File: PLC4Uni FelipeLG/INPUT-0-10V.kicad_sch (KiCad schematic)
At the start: 3 parts

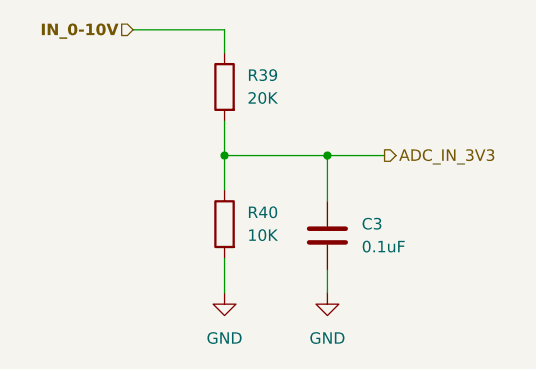
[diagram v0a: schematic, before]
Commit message: Add files via upload
Updated Circuitos corregidos y pistas agregadas
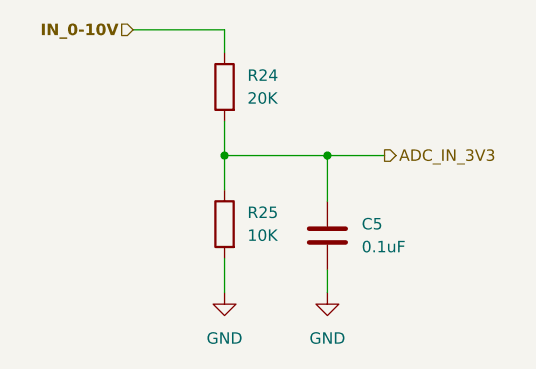
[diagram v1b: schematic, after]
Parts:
- renumbered C3 to C5, R39 to R24, R40 to R25
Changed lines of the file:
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@@
 		(dnp no)
 		(fields_autoplaced yes)
-		(property "Reference" "#PWR04"
+		(property "Reference" "#PWR049"
 			(at 133.35 121.92 0)
 			(effects
@@
 			(project "Diseños de circuitos"
 				(path "/65c875c0-73bd-43df-b6cd-4a685398cace/3b453a73-5bb7-4645-a7e8-6e186968fa05/26d79baa-0338-43a5-b3e5-bc5aeada5ecf"
-					(reference "#PWR04")
+					(reference "#PWR049")
 					(unit 1)
 				)
@@
 		(dnp no)
 		(fields_autoplaced yes)
-		(property "Reference" "R40"
+		(property "Reference" "R25"
 			(at 124.46 106.6799 0)
 			(effects
@@
 			(project "Diseños de circuitos"
 				(path "/65c875c0-73bd-43df-b6cd-4a685398cace/3b453a73-5bb7-4645-a7e8-6e186968fa05/26d79baa-0338-43a5-b3e5-bc5aeada5ecf"
-					(reference "R40")
+					(reference "R25")
 					(unit 1)
 				)
@@
 		(dnp no)
 		(fields_autoplaced yes)
-		(property "Reference" "R39"
+		(property "Reference" "R24"
 			(at 124.46 91.4399 0)
 			(effects
@@
 			(project "Diseños de circuitos"
 				(path "/65c875c0-73bd-43df-b6cd-4a685398cace/3b453a73-5bb7-4645-a7e8-6e186968fa05/26d79baa-0338-43a5-b3e5-bc5aeada5ecf"
-					(reference "R39")
+					(reference "R24")
 					(unit 1)
 				)
@@
 		(dnp no)
 		(fields_autoplaced yes)
-		(property "Reference" "#PWR01"
+		(property "Reference" "#PWR048"
 			(at 121.92 121.92 0)
 			(effects
@@
 			(project "Diseños de circuitos"
 				(path "/65c875c0-73bd-43df-b6cd-4a685398cace/3b453a73-5bb7-4645-a7e8-6e186968fa05/26d79baa-0338-43a5-b3e5-bc5aeada5ecf"
-					(reference "#PWR01")
+					(reference "#PWR048")
 					(unit 1)
 				)
@@
 		(dnp no)
 		(fields_autoplaced yes)
-		(property "Reference" "C3"
+		(property "Reference" "C5"
 			(at 137.16 107.9499 0)
 			(effects
@@
 			(project "Diseños de circuitos"
 				(path "/65c875c0-73bd-43df-b6cd-4a685398cace/3b453a73-5bb7-4645-a7e8-6e186968fa05/26d79baa-0338-43a5-b3e5-bc5aeada5ecf"
-					(reference "C3")
-					(unit 1)
-				)
+					(reference "C5")
+					(unit 1)
+				)
